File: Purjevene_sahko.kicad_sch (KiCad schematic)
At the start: 24 parts, among them J1 Conn_Coaxial, J2 Conn_01x01_Socket, J3 Conn_01x01_Socket, J4 Conn_01x01_Pin, J5 Conn_01x01_Pin, M1 Motor_AC, M2 Autopilot, SW1 Main_switch, SW2 Switchboard

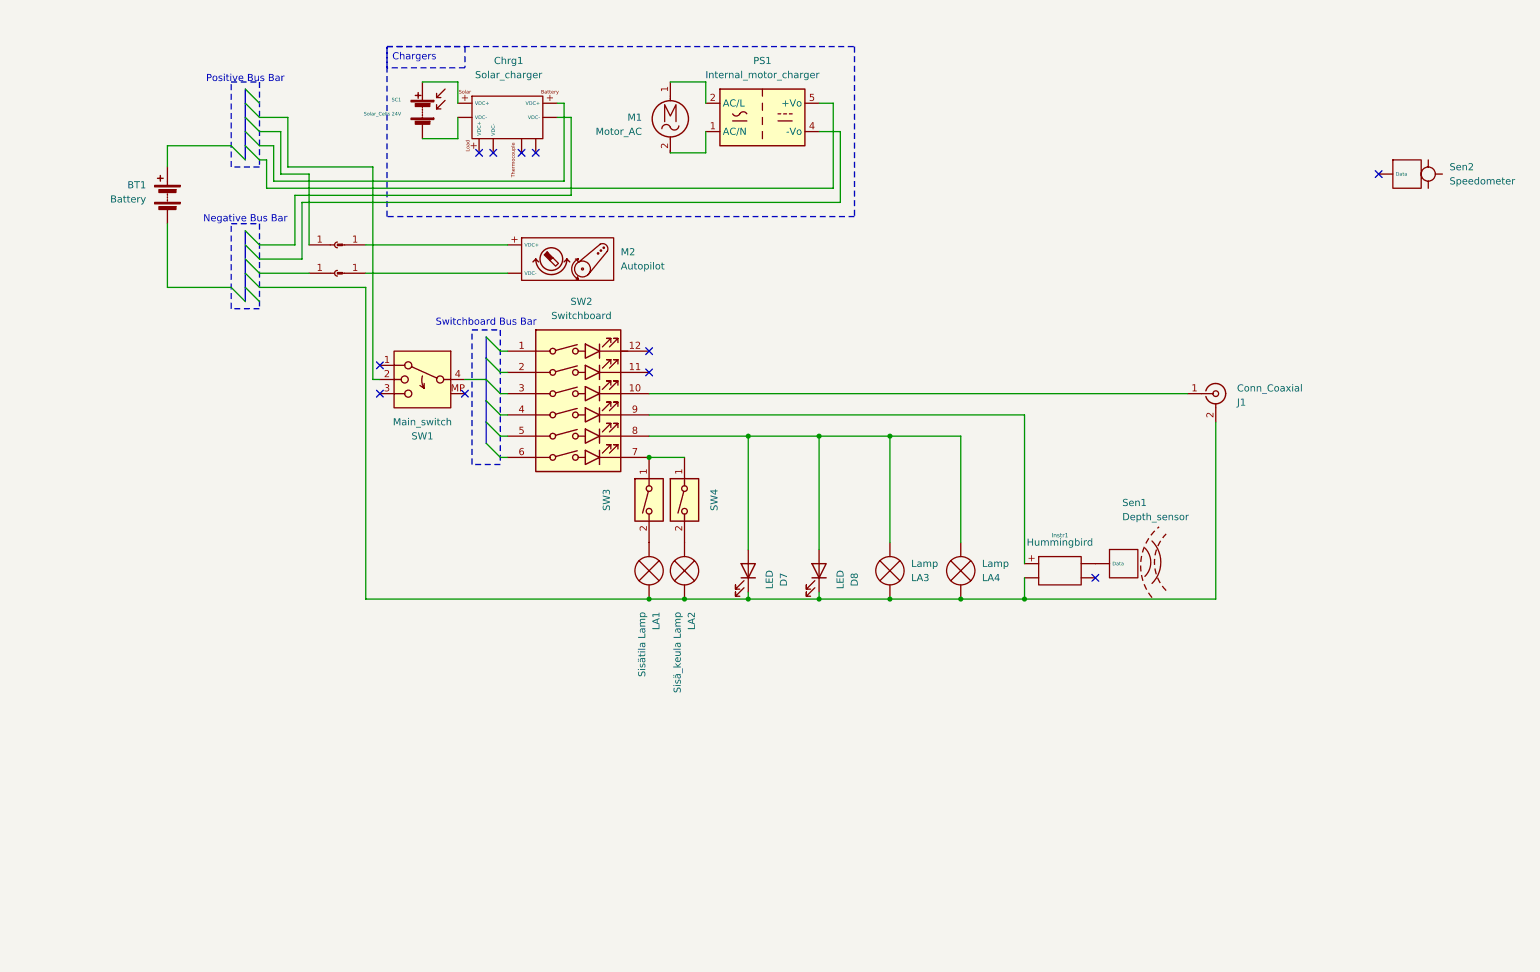
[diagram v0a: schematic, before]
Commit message: Spring 2026
First implementation of battery in bow system.
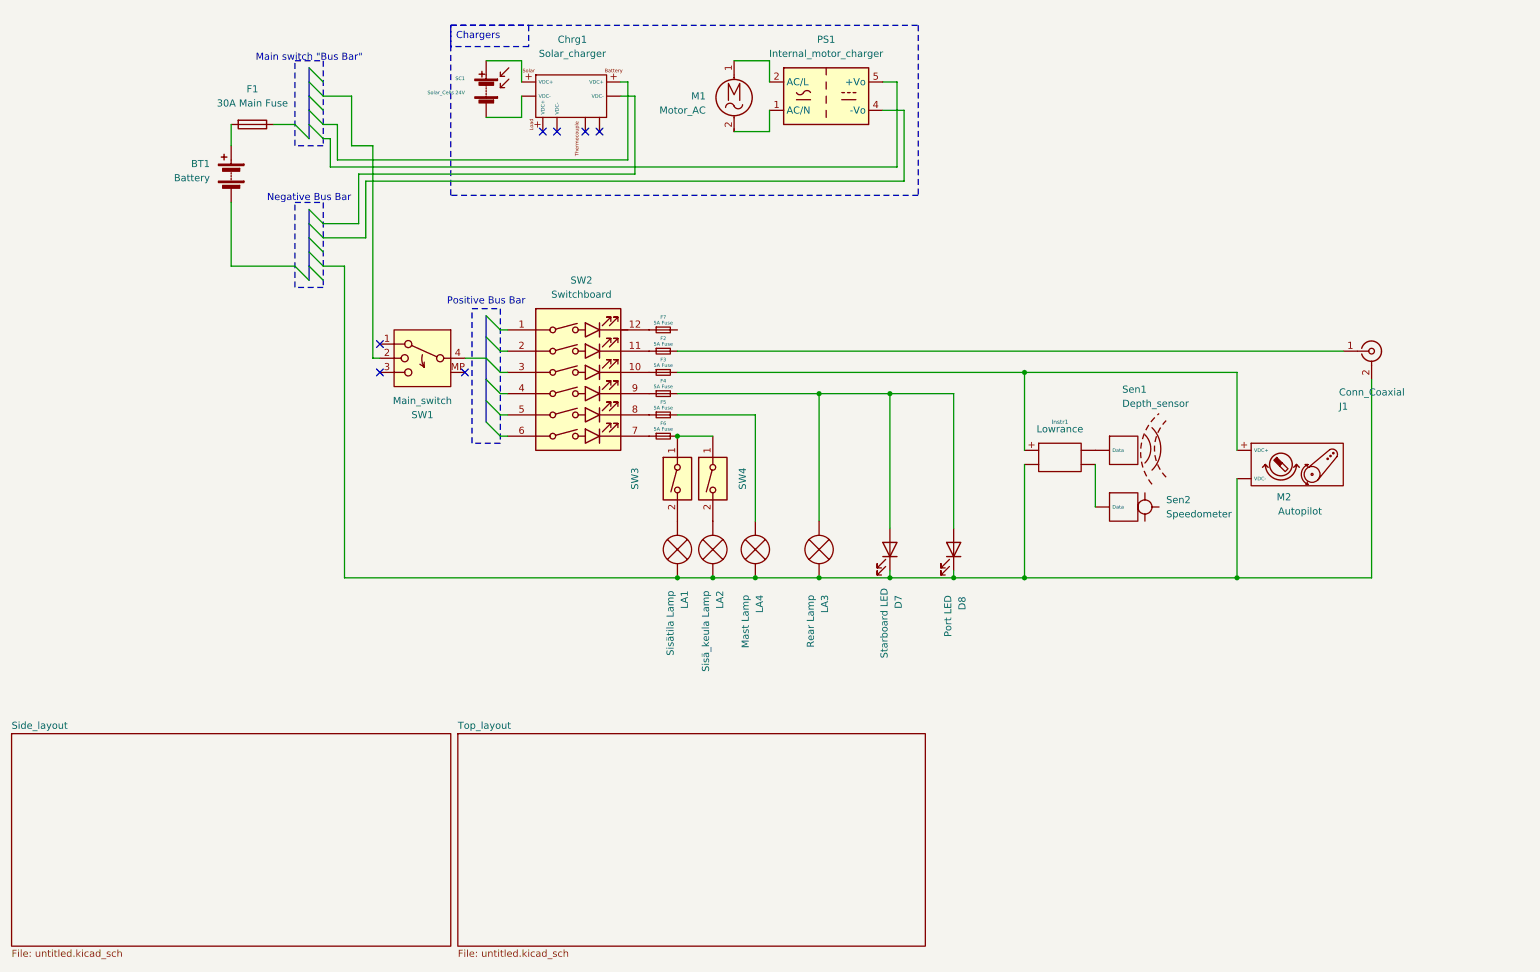
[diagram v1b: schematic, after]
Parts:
- removed J2, J3: Conn_01x01_Socket, symbol Connector:Conn_01x01_Socket
- removed J4, J5: Conn_01x01_Pin, symbol Connector:Conn_01x01_Pin
- added F1: 30A Main Fuse, symbol Device:Fuse
- added F2, F3, F4, F5, F6, F7: 5A Fuse, symbol Device:Fuse_Small
- D7: value LED -> Starboard LED
- D8: value LED -> Port LED
- Instr1: value Hummingbird -> Lowrance
- LA3: value Lamp -> Rear Lamp
- LA4: value Lamp -> Mast Lamp
- SW3, SW4: value ~ -> (none)
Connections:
- net at SW2.10: now also F3.1; no longer J1.1 (In)
- net at SW2.11: now also F2.1
- net at SW2.12: now also F7.1
- net at SW3.1, SW4.1: now also F6.2; no longer SW2.7
- net at D7.2 (A), D8.2 (A), LA3.1 (-): now also F4.2; no longer LA4.1 (-), SW2.8
- net at SW2.9: now also F4.1; no longer Instr1.+
- net at D7.1 (K), D8.1 (K), Instr1.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: now also M2. (VDC-)
- net at M2.+ (VDC+): now also Instr1.+, F3.2
- net at Instr1.: now also Sen1. (Data)
- net at Chrg1. (VDC-): now also SC1.2 (-)
- net at Chrg1.+ (VDC+): now also SC1.1 (+)
- net at Sen2. (Data): now also Instr1.
- net at BT1.1 (+): now also F1.2
- new net: F6.1, SW2.7
- new net: F5.1, SW2.8
- new net: F2.2, J1.1 (In)
- new net: F5.2, LA4.1 (-)
- no-connect marks 11 -> 7
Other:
- added sheet Side_layout (untitled.kicad_sch)
- added sheet Top_layout (untitled.kicad_sch)
- note added: "Main switch "Bus Bar""
- note removed: "Switchboard Bus Bar"
- title: (none) -> Planned schematic
- moved on the sheet: BT1, Chrg1, D7, D8, Instr1, J1, LA1, LA2, LA3, LA4, M1, M2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

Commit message: Switchboard update
Updated switchboard to a schematic that it is on the boat. Also added a pull-down line to the negative.
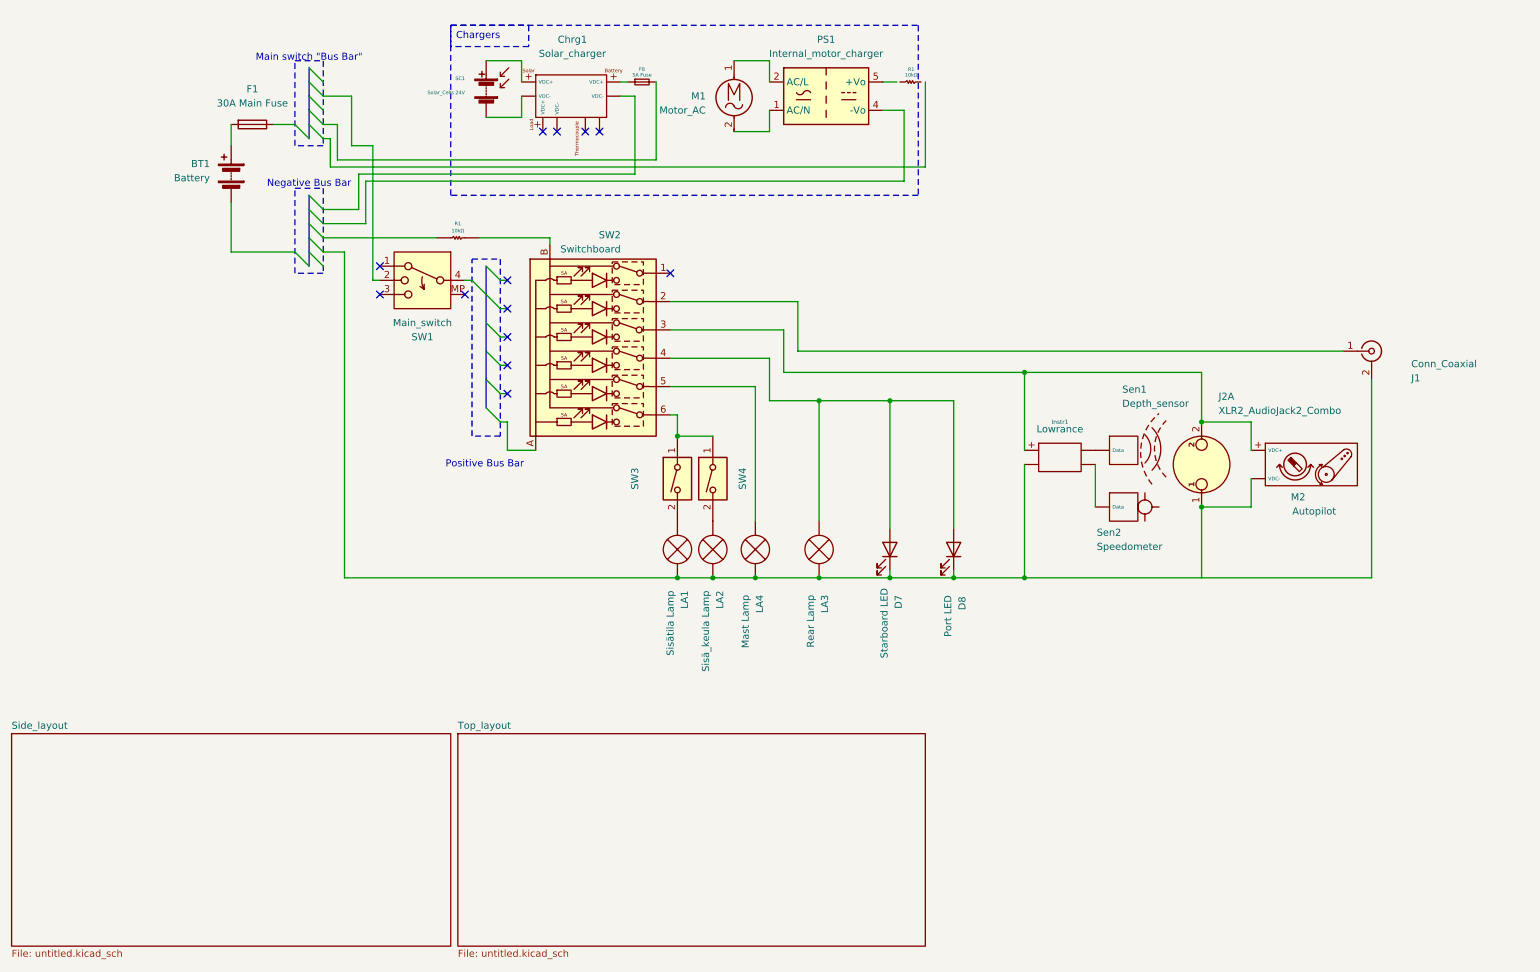
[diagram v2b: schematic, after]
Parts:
- removed F2, F3, F4, F5, F6, F7: 5A Fuse, symbol Device:Fuse_Small
- added F8: 5A Fuse, symbol Device:Fuse_Small
- added J2: XLR2_AudioJack2_Combo, symbol Connector_Audio:XLR3_AudioJack2_Combo
- added R1: 10kΩ, symbol Device:Fuse_Small
- added R1: 10kΩ, symbol Own:Resistor_10k
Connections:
- net at SW2.2: now also J1.1 (In)
- net at SW2.3: now also Instr1.+, M2.+ (VDC+), J2.2
- net at SW2.4: now also D7.2 (A), D8.2 (A), LA3.1 (-)
- net at SW2.5: now also LA4.1 (-)
- net at SW2.6: now also SW3.1, SW4.1
- net at D7.1 (K), D8.1 (K), Instr1.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: no longer M2. (VDC-)
- net at Chrg1. (VDC-): now also SC1.2 (-)
- net at Chrg1.+ (VDC+): now also SC1.1 (+)
- new net: Chrg1.+ (VDC+), F8.1
- new net: J2.1, M2. (VDC-)
- new net: R1., SW2.B
- no-connect marks 7 -> 13
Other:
- moved on the sheet: M2, SW1

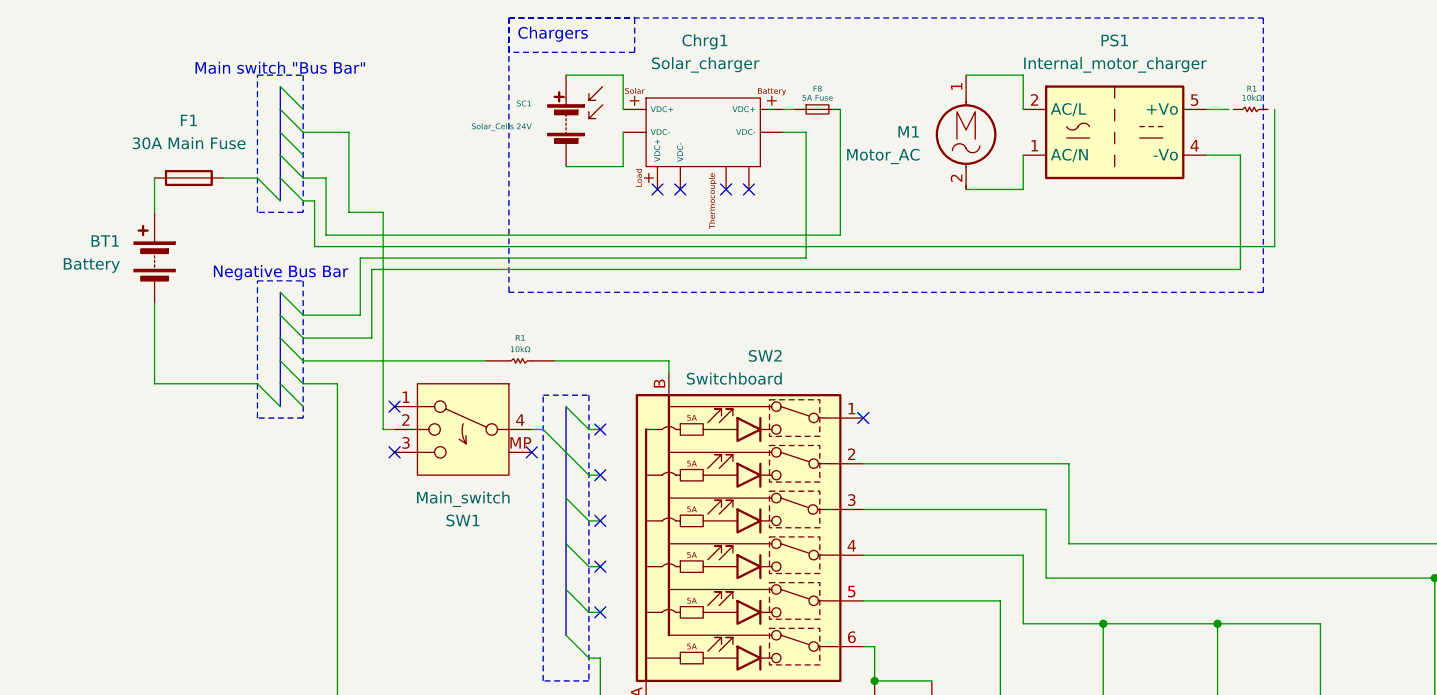
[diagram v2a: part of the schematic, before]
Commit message: Main switch
Updated main switch to reality.
This also removed the temporary positive bar to connect chargers. They are now connected to main switch.
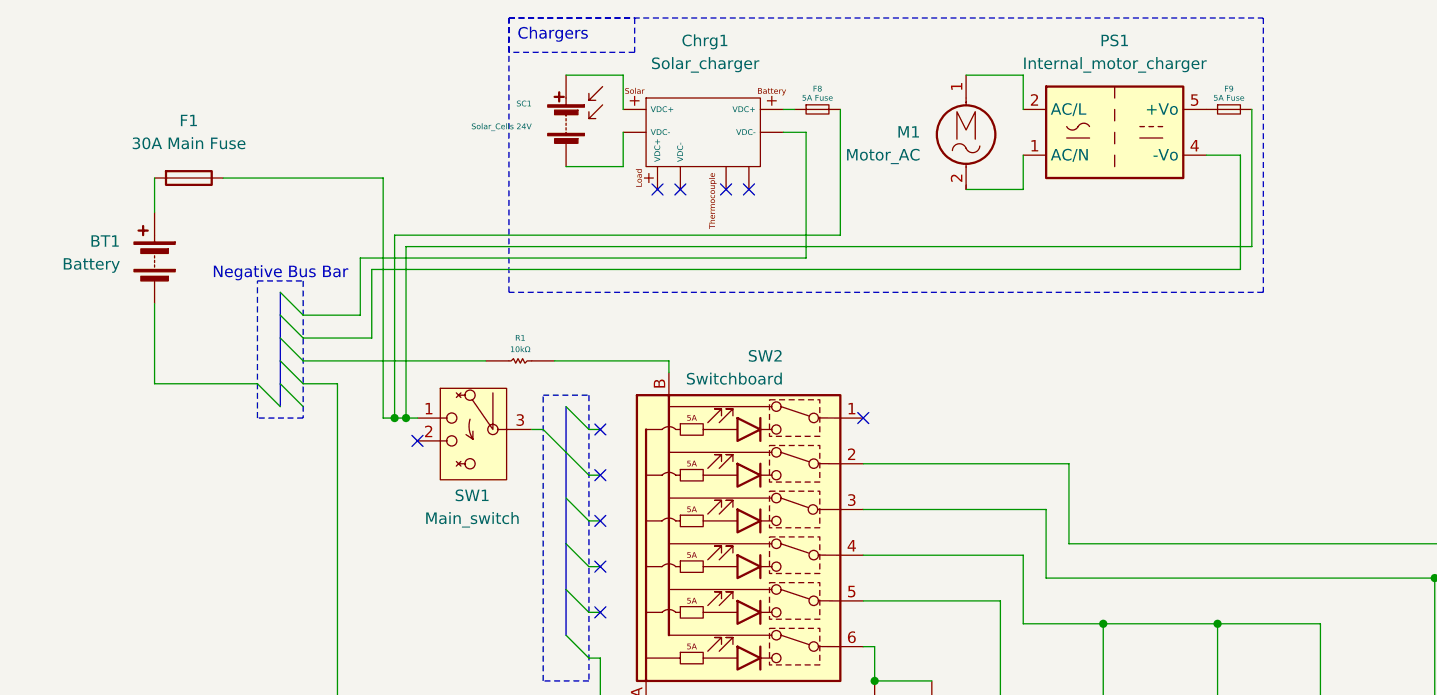
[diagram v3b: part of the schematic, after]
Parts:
- removed R1: 10kΩ, symbol Device:Fuse_Small
- removed SW1: Main_switch, symbol Switch:SW_Rotary_1x3_MP
- added F9: 5A Fuse, symbol Device:Fuse_Small
- added SW1: Main_switch, symbol Own:SW_Rotary_1x3_MP
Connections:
- net at F1.1: now also F8.2, F9.2, SW1.1
- net at Chrg1. (VDC-): now also SC1.2 (-)
- net at Chrg1.+ (VDC+): now also SC1.1 (+)
- net at PS1.5 (+Vo): now also F9.1
- no-connect marks 13 -> 11
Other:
- note removed: "Main switch "Bus Bar""

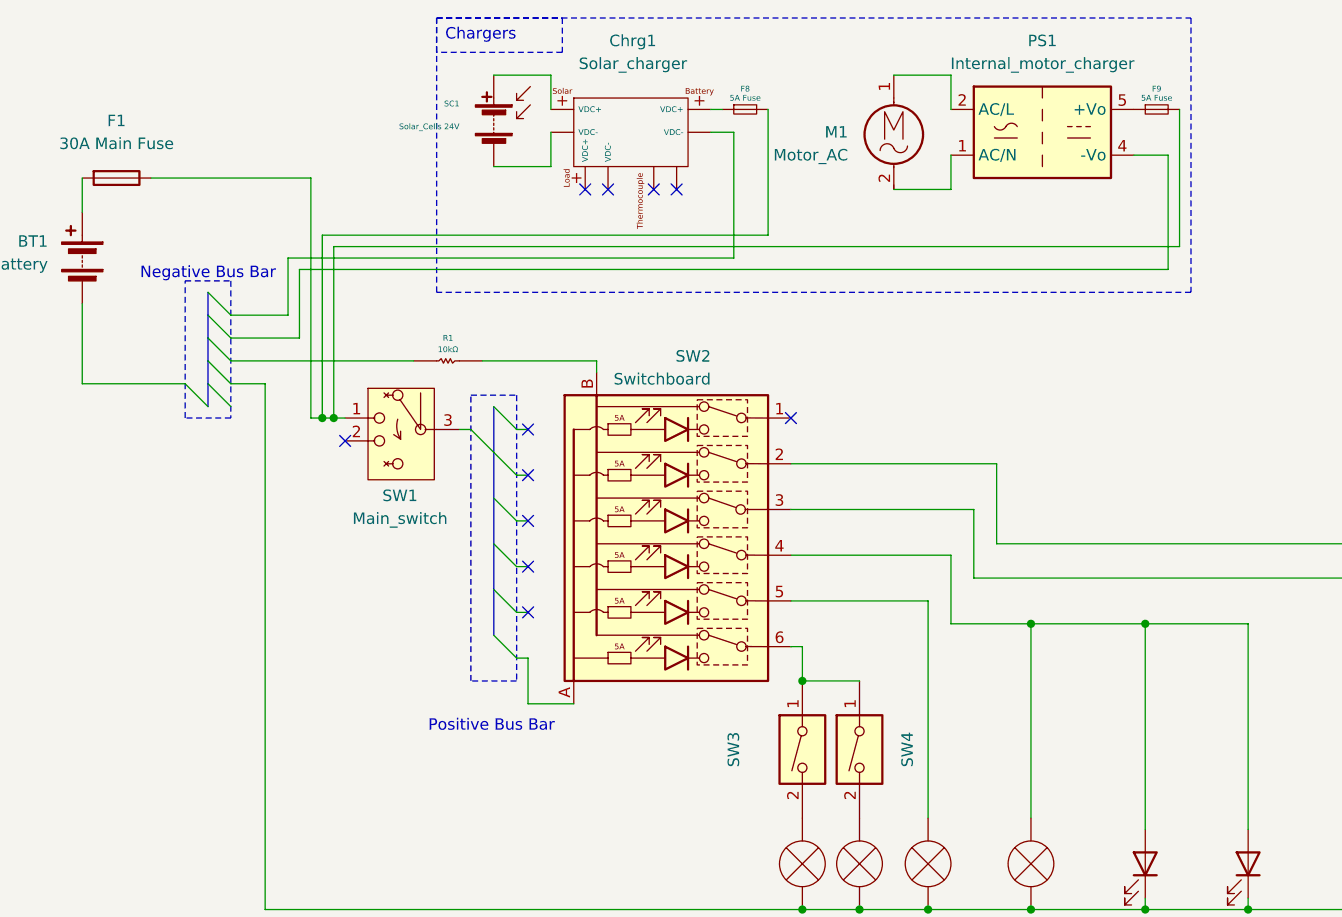
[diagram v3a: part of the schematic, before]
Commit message: Cable sizes
Added cable size description and line width to the schematics
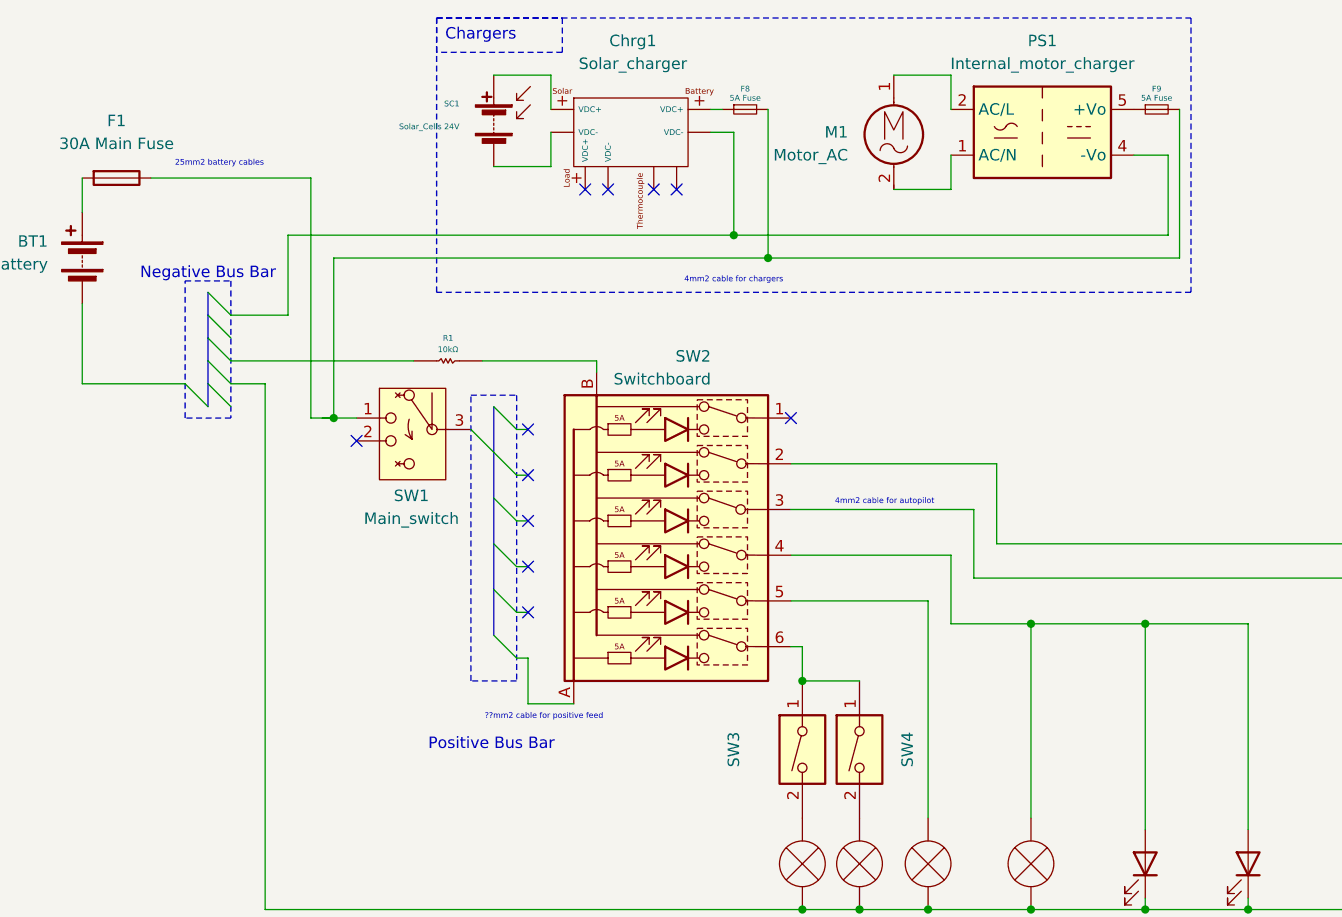
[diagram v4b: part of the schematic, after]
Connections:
- net at Chrg1. (VDC-): now also PS1.4 (-Vo)
- net at Chrg1.+ (VDC+): now also SC1.1 (+)
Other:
- note added: "25mm2 battery cables"
- note added: "4mm2 cable for autopilot"
- note added: "4mm2 cable for chargers"
- note added: "??mm2 cable for positive feed"
- moved on the sheet: SW1
